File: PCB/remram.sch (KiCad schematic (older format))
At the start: 0 parts

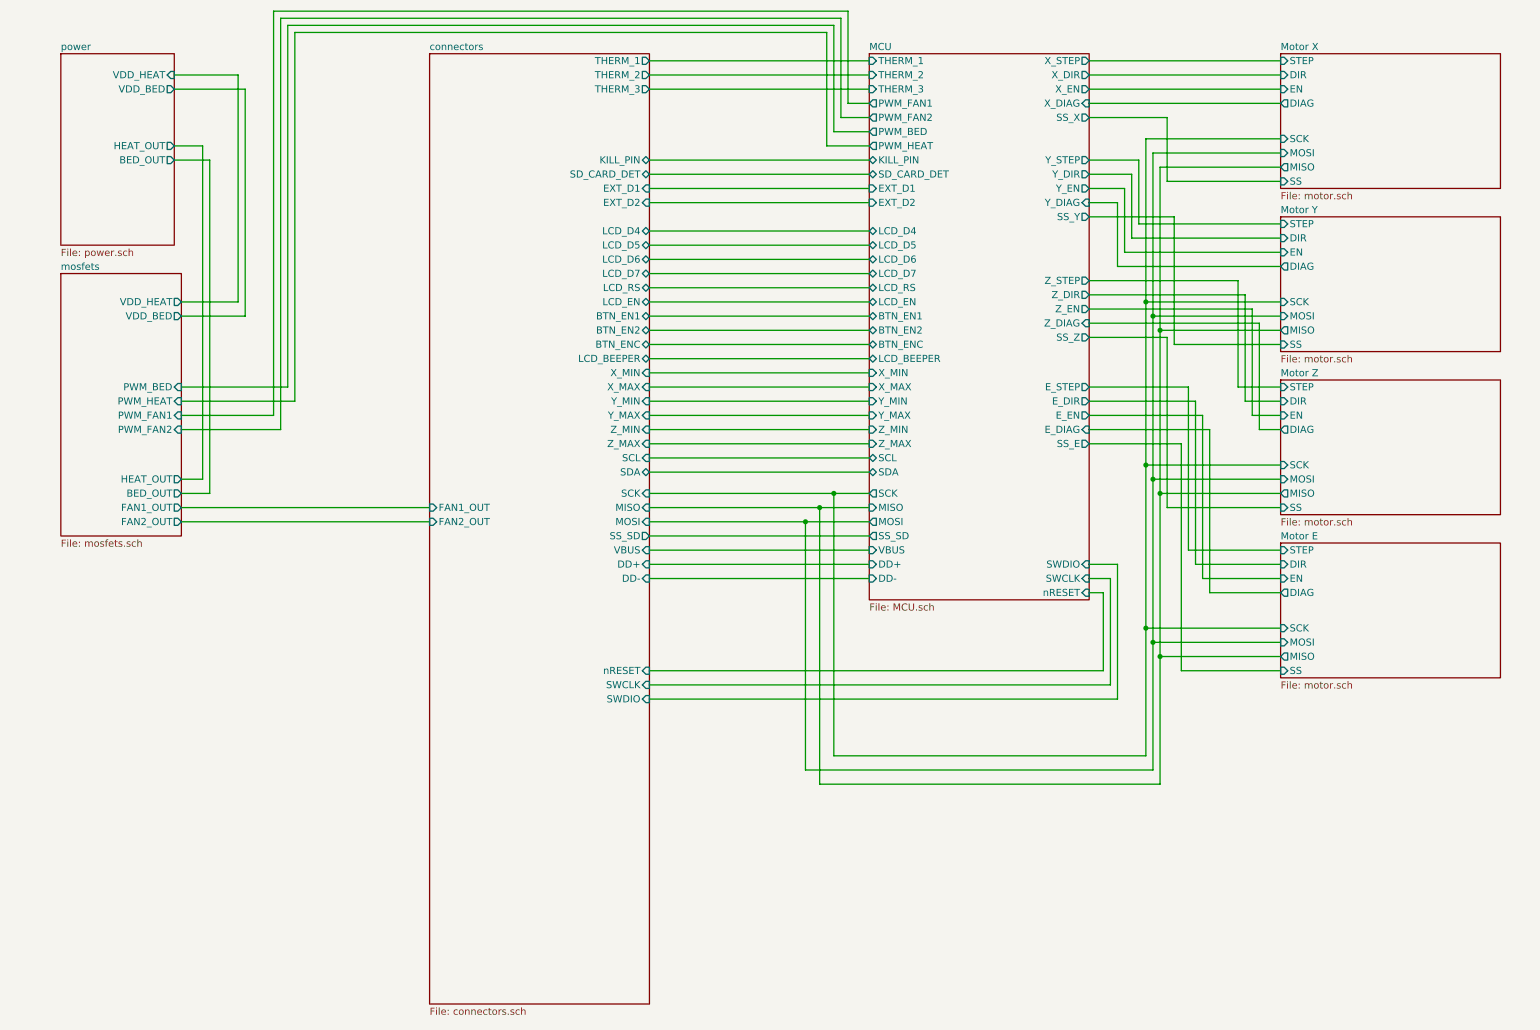
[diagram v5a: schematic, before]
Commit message: Added the secnd Z connection.
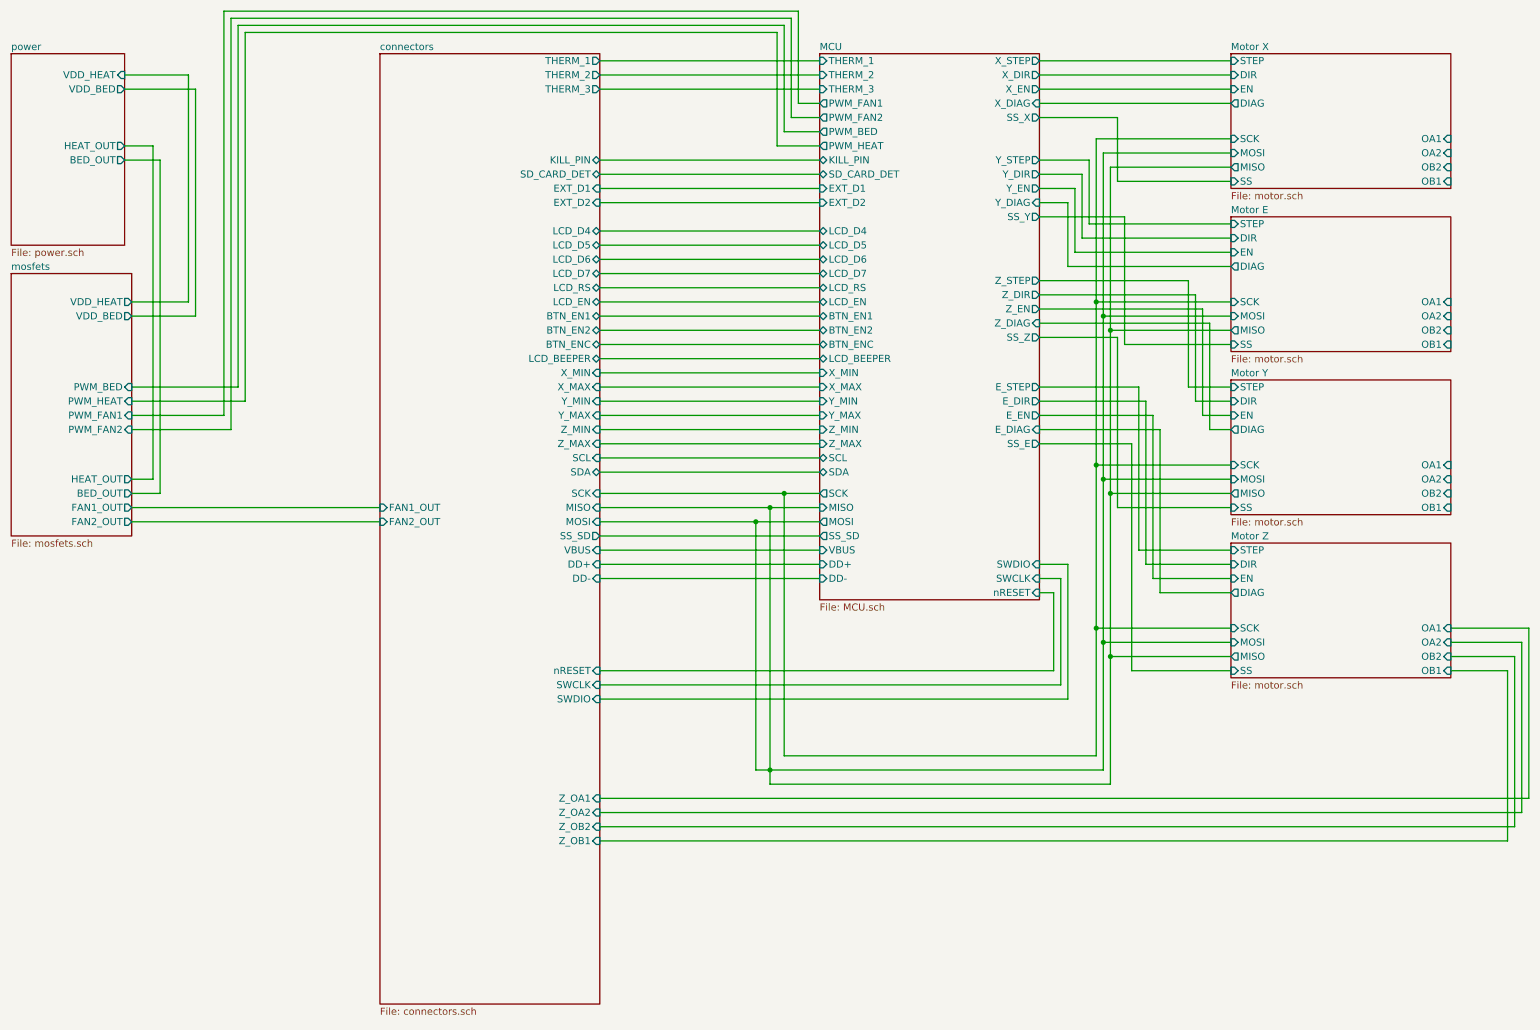
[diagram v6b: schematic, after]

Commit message: First PCB version that is fully placed and routed.
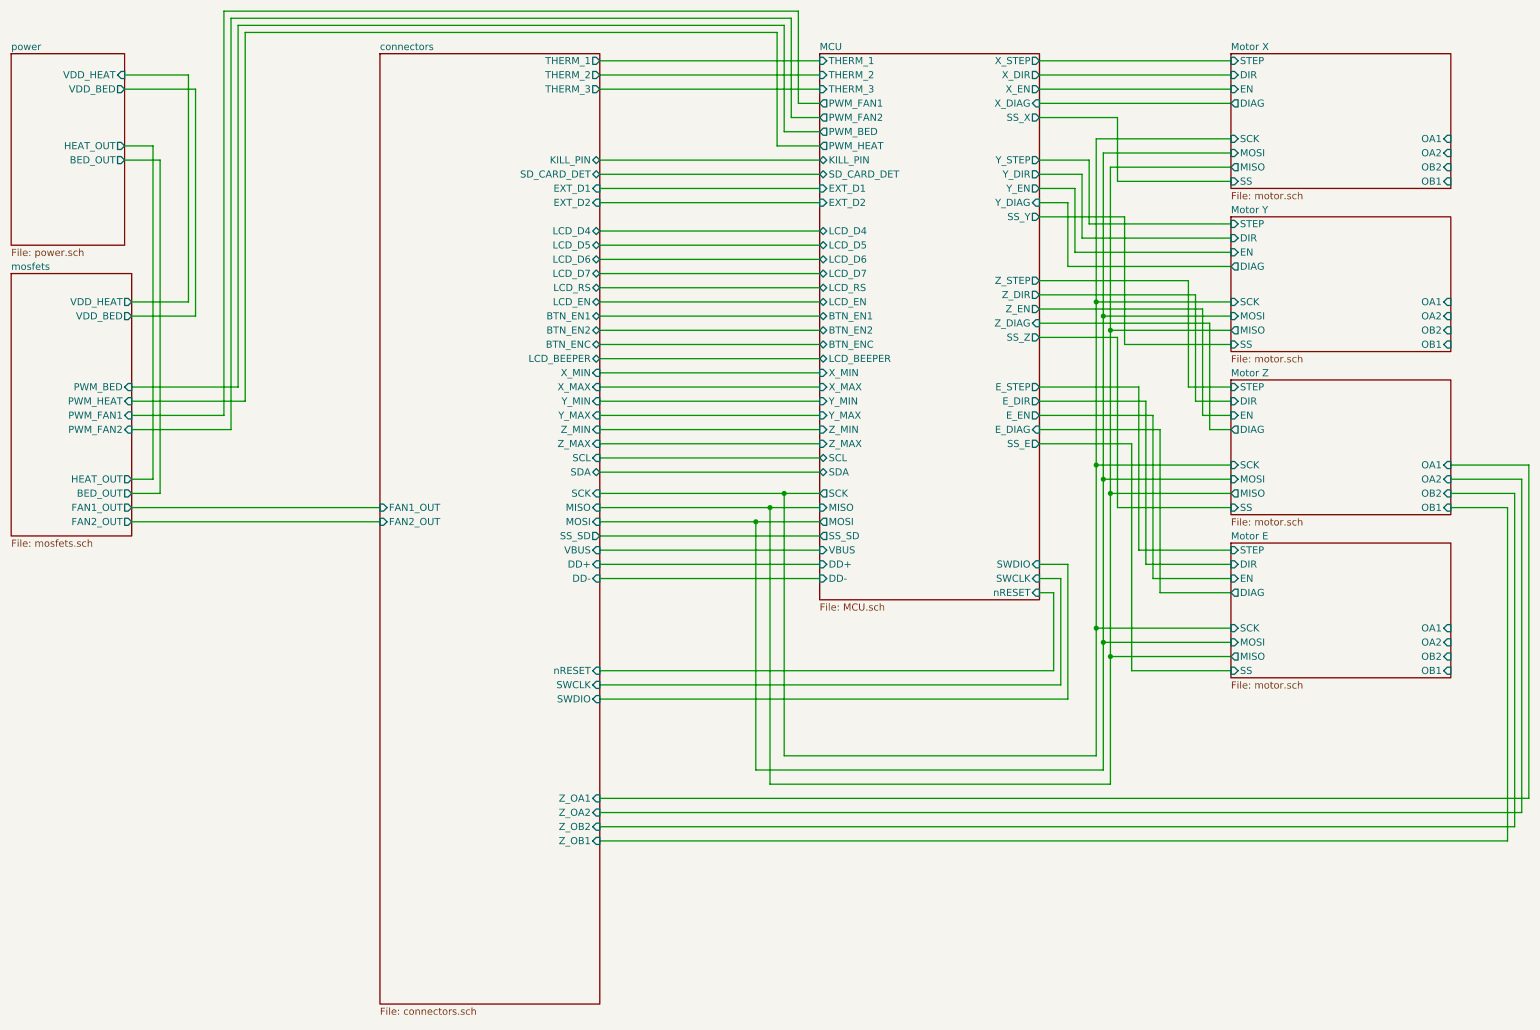
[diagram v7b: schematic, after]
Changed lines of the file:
@@
 Wire Wire Line
 	5950 5800 8150 5800
-Wire Wire Line
-	5850 4050 5850 5900
 Connection ~ 5850 4050
 Wire Wire Line
@@
 Wire Wire Line
 	5750 4150 6200 4150
-Wire Wire Line
-	5850 6000 5850 5900
 Wire Wire Line
 	5850 6000 8250 6000
@@
 $EndSheet
 $Sheet
-S 9100 2000 1550 950
+S 9100 4300 1550 950
 U 5AFC22B0
 F0 "Motor E" 50
+F1 "motor.sch" 50
+F2 "SCK" I L 9100 4900 50
+F3 "MOSI" I L 9100 5000 50
+F4 "MISO" O L 9100 5100 50
+F5 "STEP" I L 9100 4350 50
+F6 "DIR" I L 9100 4450 50
+F7 "EN" I L 9100 4550 50
+F8 "SS" I L 9100 5200 50
+F9 "DIAG" O L 9100 4650 50
+F10 "OA1" I R 10650 4900 50
+F11 "OA2" I R 10650 5000 50
+F12 "OB2" I R 10650 5100 50
+F13 "OB1" I R 10650 5200 50
+$EndSheet
+$Sheet
+S 9100 2000 1550 950
+U 5AFC9D86
+F0 "Motor Y" 50
 F1 "motor.sch" 50
 F2 "SCK" I L 9100 2600 50
@@
 $Sheet
 S 9100 3150 1550 950
-U 5AFC9D86
-F0 "Motor Y" 50
+U 5AFD185C
+F0 "Motor Z" 50
 F1 "motor.sch" 50
 F2 "SCK" I L 9100 3750 50
@@
 F13 "OB1" I R 10650 4050 50
 $EndSheet
-$Sheet
-S 9100 4300 1550 950
-U 5AFD185C
-F0 "Motor Z" 50
-F1 "motor.sch" 50
-F2 "SCK" I L 9100 4900 50
-F3 "MOSI" I L 9100 5000 50
-F4 "MISO" O L 9100 5100 50
-F5 "STEP" I L 9100 4350 50
-F6 "DIR" I L 9100 4450 50
-F7 "EN" I L 9100 4550 50
-F8 "SS" I L 9100 5200 50
-F9 "DIAG" O L 9100 4650 50
-F10 "OA1" I R 10650 4900 50
-F11 "OA2" I R 10650 5000 50
-F12 "OB2" I R 10650 5100 50
-F13 "OB1" I R 10650 5200 50
-$EndSheet
 Wire Wire Line
 	11200 6100 4650 6100
@@
 Wire Wire Line
 	11050 6400 4650 6400
-Connection ~ 5850 5900
 Wire Wire Line
 	5850 5900 8200 5900
 Wire Wire Line
-	11200 6100 11200 4900
-Wire Wire Line
-	11200 4900 10650 4900
-Wire Wire Line
-	10650 5000 11150 5000
-Wire Wire Line
-	11150 5000 11150 6200
-Wire Wire Line
-	11100 6300 11100 5100
-Wire Wire Line
-	11100 5100 10650 5100
-Wire Wire Line
-	10650 5200 11050 5200
-Wire Wire Line
-	11050 5200 11050 6400
+	11200 3750 10650 3750
+Wire Wire Line
+	11200 3750 11200 6100
+Wire Wire Line
+	10650 3850 11150 3850
+Wire Wire Line
+	11150 3850 11150 6200
+Wire Wire Line
+	11100 3950 10650 3950
+Wire Wire Line
+	11100 3950 11100 6300
+Wire Wire Line
+	10650 4050 11050 4050
+Wire Wire Line
+	11050 4050 11050 6400
+Wire Wire Line
+	5850 4050 5850 6000
 $EndSCHEMATC
